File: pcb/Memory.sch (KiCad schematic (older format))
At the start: 8 parts, among them U5 SDRAM

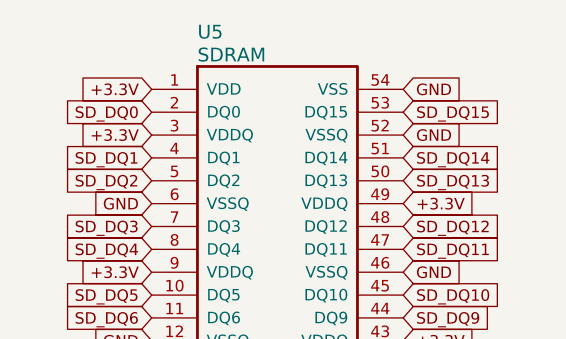
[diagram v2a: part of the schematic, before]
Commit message: Added manufacturer part numbers to the schematic.
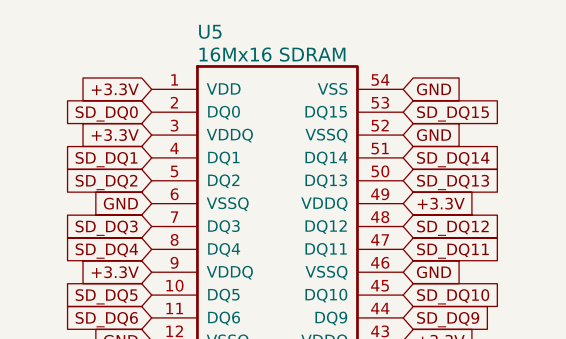
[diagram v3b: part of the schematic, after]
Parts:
- C8: manf# (none) -> GRM188R71C104KA01D
- U5: value SDRAM -> 16Mx16 SDRAM
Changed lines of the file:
@@
 P 5500 2500
 F 0 "U5" H 5700 2750 60  0000 L CNN
-F 1 "SDRAM" H 5700 2650 60  0000 L CNN
+F 1 "16Mx16 SDRAM" H 5700 2650 60  0000 L CNN
 F 2 "XESS:TSOPII-54" H 5500 2500 60  0001 C CNN
 F 3 "" H 5500 2500 60  0000 C CNN
@@
 F 2 "Capacitors_SMD:C_0603" H 5188 5600 30  0001 C CNN
 F 3 "" H 5150 5750 60  0000 C CNN
+F 4 "GRM188R71C104KA01D" H 5150 5750 60  0001 C CNN "manf#"
 	1    5150 5750
 	1    0    0    -1
@@
 1E 25 49 2A DA F6 C4 5C B7 0C C3 B9 A4 0A 98 09 FC 0D B0 92 CD 57 CD 1F 06 4E 04 26 A7 75 27 49
 52 39 26 13 73 DE C3 6C BE 70 B5 12 F8 16 86 73 8D C3 FF 03 63 F8 EE 2E BE 9A 04 B1 00 00 00 00
-49 45 4E 44 AE 42 60 82 40
+49 45 4E 44 AE 42 60 82 13
 EndData
 $EndBitmap
